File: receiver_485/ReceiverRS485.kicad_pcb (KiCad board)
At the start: 2 copper layers, 69.2 x 100 mm, 93 parts, among them J1 USB3_A, J2 Conn_01x03, J3 USB3_A, J4 Conn_01x03, J5 USB3_A, J6 Conn_01x03, J7 USB3_A, J8 Conn_01x03, U1 RFM-0505S, U10 MAX3283E, U11 TLP2372, U12 TLP2372, U13 RFM-0505S, U14 MAX3283E, U15 TLP2372, U16 MAX3283E, U17 TLP2372, U18 TLP2372, U19 RFM-0505S, U2 MAX3283E, U20 MAX3283E, U21 TLP2372, U22 MAX3283E, U23 TLP2372, U24 TLP2372, U25 USB3_duplo, U26 USB3_duplo, U3 TLP2372, U4 MAX3283E, U5 TLP2372, U6 TLP2372, U7 RFM-0505S, U8 MAX3283E, U9 TLP2372

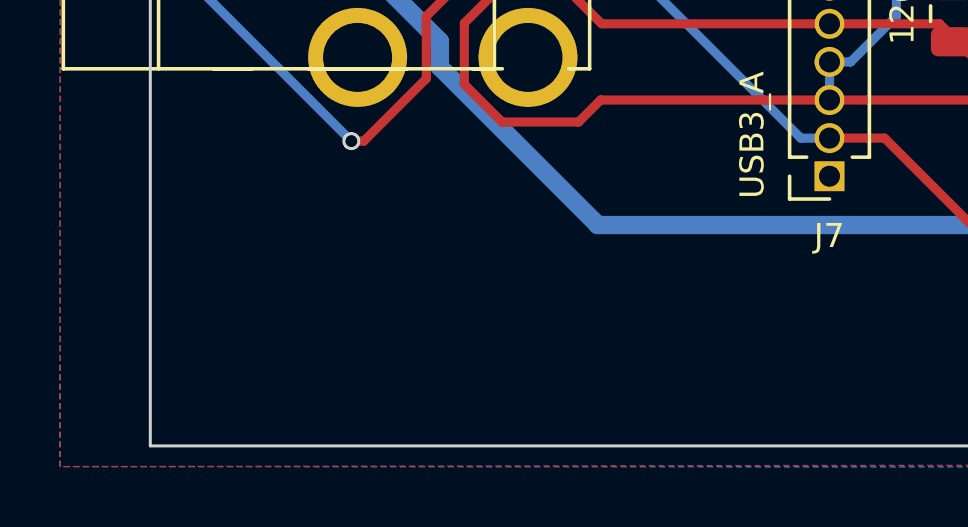
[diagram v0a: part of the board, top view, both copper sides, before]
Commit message: New PCB of the Adapter
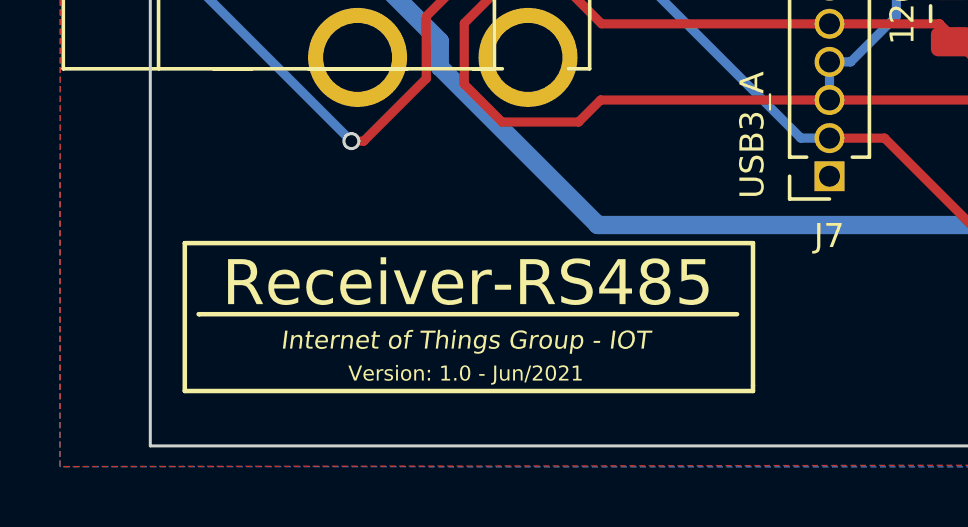
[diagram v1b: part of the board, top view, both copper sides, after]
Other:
- board text added: "Internet of Things Group - IOT"
- board text added: "Receiver-RS485"
- board text added: "Version: 1.0 - Jun/2021"

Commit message: update receiver pcb
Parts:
- renumbered U26 to J10, U25 to J9
